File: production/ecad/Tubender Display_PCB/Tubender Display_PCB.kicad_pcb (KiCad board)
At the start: 2 copper layers, 2 parts, among them J1 4-1734592-0, J2 4-1734592-0

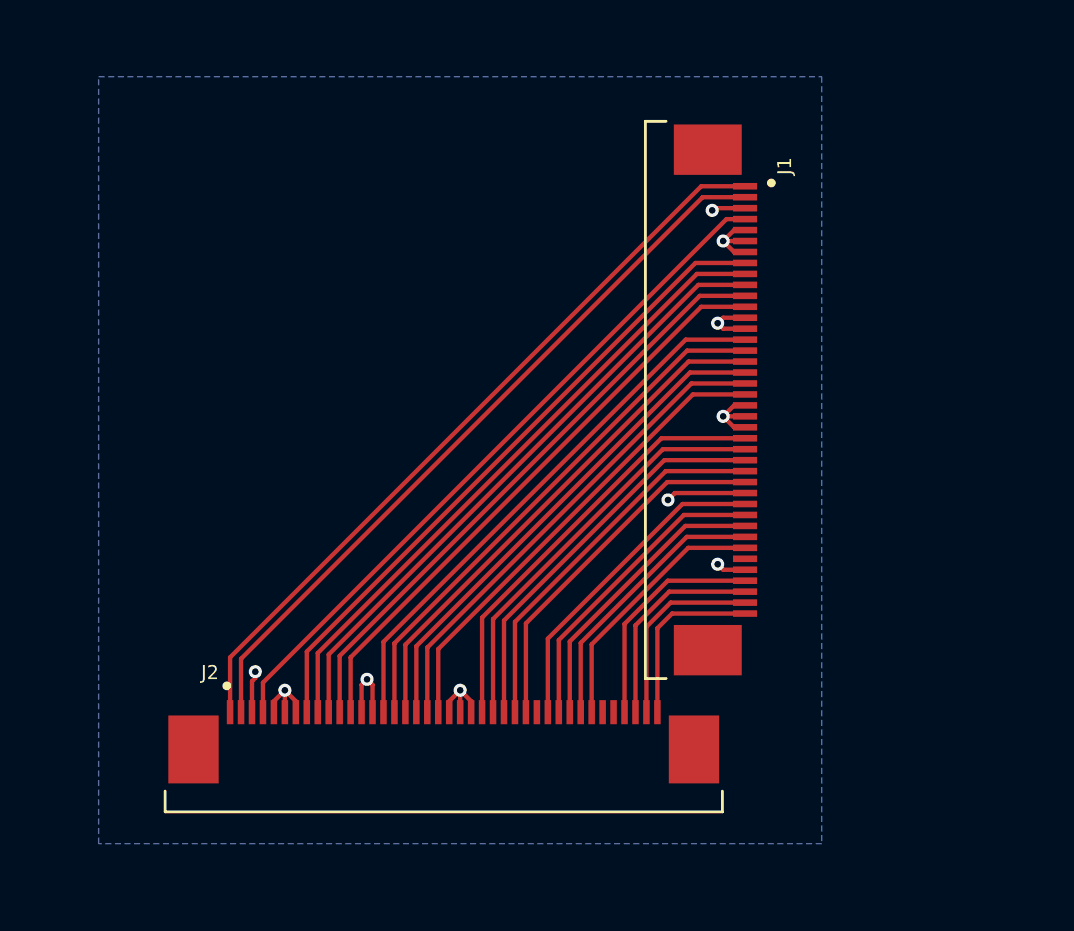
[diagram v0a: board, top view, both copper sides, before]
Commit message: Fixed daughter board DRC issues
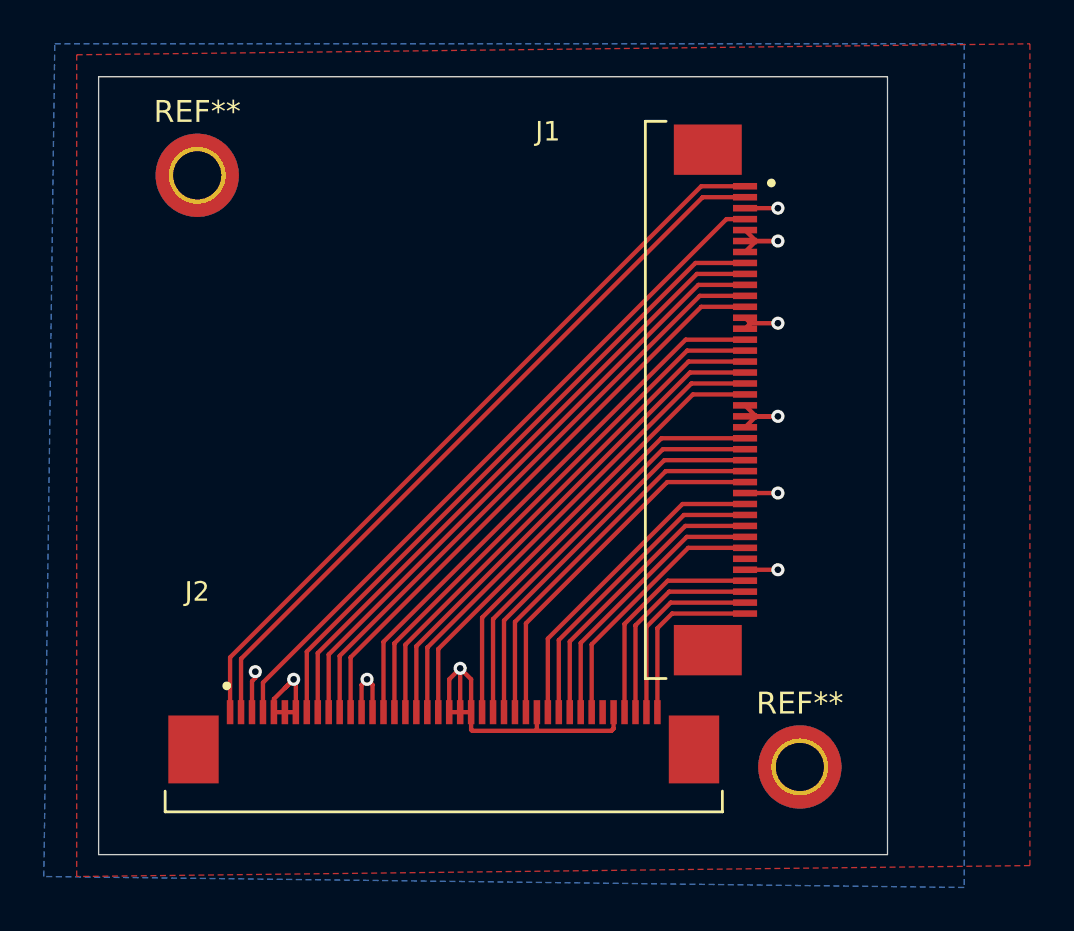
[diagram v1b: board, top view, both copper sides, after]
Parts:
- added REF**: MountingHole_2.2mm_M2_DIN965_Pad_TopBottom, MountingHole:MountingHole_2.2mm_M2_DIN965_Pad_TopBottom, F.Cu at (163.0, 110.5)
- added REF**: MountingHole_2.2mm_M2_DIN965_Pad_TopBottom, MountingHole:MountingHole_2.2mm_M2_DIN965_Pad_TopBottom, F.Cu at (135.5, 83.5)
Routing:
- net GND: track 28.0 -> 40.8 mm
- added copper zone on F.Cu, net GND
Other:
- board outline added: 36 x 35.5 mm
